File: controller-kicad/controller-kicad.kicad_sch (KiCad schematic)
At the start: 97 parts

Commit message: Finishing up ECU schematic
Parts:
- removed C? (x3): 10nF, symbol Device:C_Small
- removed R?: 10K, symbol Device:R_Small
- removed U?: PC817, Package_DIP:DIP-4_W7.62mm, symbol Isolator:PC817
- removed U?: MCP1416, Package_TO_SOT_SMD:SOT-23-5, symbol Driver_FET:MCP1416
- added C1, C2: 27pF, symbol Device:C_Small
- added C24, C26, C28, C36, C38: 10nF, symbol Device:C_Small
- added C31, C32, C33, C34: 10pF DNP, symbol Device:C_Small
- added C35: 22nF, symbol Device:C_Small
- added C37: 100nF, symbol Device:C_Small
- added FB1, FB2: FerriteBead_Small, symbol Device:FerriteBead_Small
- added J1: RJ45_Amphenol_RJMG1BD3B8K1ANR, Connector_RJ:RJ45_Amphenol_RJMG1BD3B8K1ANR, symbol Connector:RJ45_Amphenol_RJMG1BD3B8K1ANR
- added J11: Conn_01x02_Female, symbol Connector:Conn_01x02_Female
- added R22: 1.5K, symbol Device:R_Small
- added R24: 750, symbol Device:R_Small
- added R32: 1K, symbol Device:R_Small
- added R33: 1M, symbol Device:R_Small
- added R34: 350, symbol Device:R_Small
- added U11: TL431DBZ, Package_TO_SOT_SMD:SOT-23, symbol Reference_Voltage:TL431DBZ
- added U12: AD8495, Package_SO:MSOP-8_3x3mm_P0.65mm, symbol Sensor_Temperature:AD8495
- added U13: TLP250, Package_DIP:DIP-8_W7.62mm, symbol Driver_FET:TLP250
- added Y1: 25 MHz, symbol Device:Crystal
- gave numbers to parts that had none: 91
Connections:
- net +3.3V: now also C24.1, C26.1, C28.1, C35.2, FB2.2, J1.R4 (TCT), J1.R5 (RCT), R24.2, R32.2, U12.7 (+Vs); no longer C42.1, U15.2 (VO)
- net +5V: now also FB1.2; no longer C41.1, U14.2 (VO)
- net ADC3_IN7: now also U12.5 (SENSE), U12.6
- net ADC3_IN8: now also R22.1, R24.1
- net ETH_LED1: now also J1.L4 (LEDG_A)
- net ETH_LED2: now also J1.L1 (LEDY_A)
- net GND: now also C1.1, C2.1, C24.2, C26.2, C28.2, C31.2, C32.2, C33.2, C34.2, C35.1, C36.1, C38.2, J1.L2 (LEDY_K), J1.L3 (LEDG_K), R22.2, R33.2, U11.3 (A), U12.3 (-Vs), U13.3 (C)
- net SPARK: now also U13.6 (VO)
- net SPARK_CTRL: now also R34.1
- net SPARK_GND: now also U13.5 (VEE)
- net SPARK_VCC: now also U13.8 (VCC)
- net Vdrive: now also J4.2 (Pin_2), J5.2 (Pin_2)
- net at R23.2, U6.20 (TXN): now also C31.1, J1.R2 (TD-)
- net at R25.2, U6.21 (TXP): now also C32.1, J1.R1 (TD+)
- net at R28.2, U6.22 (RXN): now also C33.1, J1.R6 (RD-)
- net at R31.2, U6.23 (RXP): now also C34.1, J1.R3 (RD+)
- net at U1.23 (PH0): now also C1.2, Y1.2
- net at U1.24 (PH1): now also C2.2, Y1.1
- new net: R32.1, U11.1 (K), U11.2 (REF), U12.2 (REF)
- new net: C42.1, FB2.1, U15.2 (VO)
- new net: C41.1, FB1.1, U14.2 (VO)
- new net: R34.2, U13.2 (A)
- new net Earth: J1.13 (SHIELD), J1.R8 (GND)
- new net TS1+: C36.2, C37.1, J11.1 (Pin_1), U12.8 (+IN)
- new net TS1-: C37.2, C38.1, J11.2 (Pin_2), R33.1, U12.1 (-IN)
- no-connect marks 0 -> 91
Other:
- moved on the sheet: C18, C20, C21, C22, C39, C40, C41, C42, D1, D2, D3, D4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

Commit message: Started routing PCB
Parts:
- removed C13, C15: 2.2uF, symbol Device:C_Small
- removed FB2: FerriteBead_Small, symbol Device:FerriteBead_Small
- added C1, C4: 2.2uF, Capacitor_SMD:C_0603_1608Metric_Pad1.08x0.95mm_HandSolder, symbol Device:C_Small
- added J12: Conn_01x01, Connector_PinHeader_2.54mm:PinHeader_1x01_P2.54mm_Vertical, symbol Connector_Generic:Conn_01x01
- added R16: 10K, Resistor_SMD:R_0603_1608Metric_Pad0.98x0.95mm_HandSolder, symbol Device:R_Small
- C10: renamed from C8; footprint (none) -> Capacitor_SMD:C_0603_1608Metric_Pad1.08x0.95mm_HandSolder
- C11: renamed from C9; footprint (none) -> Capacitor_SMD:C_0603_1608Metric_Pad1.08x0.95mm_HandSolder
- C12: renamed from C10; footprint (none) -> Capacitor_SMD:C_0603_1608Metric_Pad1.08x0.95mm_HandSolder
- C13: renamed from C11; footprint (none) -> Capacitor_SMD:C_0603_1608Metric_Pad1.08x0.95mm_HandSolder
- C14: renamed from C12; footprint (none) -> Capacitor_SMD:C_0603_1608Metric_Pad1.08x0.95mm_HandSolder
- C15: renamed from C14; footprint (none) -> Capacitor_SMD:C_0603_1608Metric_Pad1.08x0.95mm_HandSolder
- C16, C17, C18, C19, C20, C21, C22, C23, C24, C25, C26, C27, C28, C29, C30, C31, C32, C33, C34, C35, C36, C37, C38, C39, C40, C41, C42, FB1: footprint (none) -> Capacitor_SMD:C_0603_1608Metric_Pad1.08x0.95mm_HandSolder
- C2: renamed from C1; footprint (none) -> Capacitor_SMD:C_0603_1608Metric_Pad1.08x0.95mm_HandSolder
- C3: renamed from C2; footprint (none) -> Capacitor_SMD:C_0603_1608Metric_Pad1.08x0.95mm_HandSolder
- C5: renamed from C3; footprint (none) -> Capacitor_SMD:C_0603_1608Metric_Pad1.08x0.95mm_HandSolder
- C6: renamed from C4; footprint (none) -> Capacitor_SMD:C_0603_1608Metric_Pad1.08x0.95mm_HandSolder
- C7: renamed from C5; footprint (none) -> Capacitor_SMD:C_0603_1608Metric_Pad1.08x0.95mm_HandSolder
- C8: renamed from C6; footprint (none) -> Capacitor_SMD:C_0603_1608Metric_Pad1.08x0.95mm_HandSolder
- C9: renamed from C7; footprint (none) -> Capacitor_SMD:C_0603_1608Metric_Pad1.08x0.95mm_HandSolder
- D1, D2, D5, D6: footprint (none) -> Diode_SMD:D_SMA_Handsoldering
- D3, D4, D7, D8: footprint (none) -> Diode_SMD:D_SMA-SMB_Universal_Handsoldering
- J10, J6, J7, J8, J9: footprint (none) -> Connector_JST:JST_PH_B3B-PH-K_1x03_P2.00mm_Vertical
- J11, J2, J3, J4, J5: footprint (none) -> Connector_JST:JST_PH_B2B-PH-K_1x02_P2.00mm_Vertical
- J13: renamed from J12; footprint (none) -> Connector_JST:JST_VH_B3P-VH-B_1x03_P3.96mm_Vertical
- J14: renamed from J13; footprint (none) -> Connector_JST:JST_PH_B5B-PH-K_1x05_P2.00mm_Vertical
- R1, R10, R14, R15, R2, R3, R4, R5, R8, R9: footprint (none) -> Resistor_SMD:R_0603_1608Metric_Pad0.98x0.95mm_HandSolder
- R11, R12, R13: value 10 -> 33; footprint (none) -> Resistor_SMD:R_0603_1608Metric_Pad0.98x0.95mm_HandSolder
- R17: renamed from R16; footprint (none) -> Resistor_SMD:R_0603_1608Metric_Pad0.98x0.95mm_HandSolder
- R18: renamed from R17; footprint (none) -> Resistor_SMD:R_0603_1608Metric_Pad0.98x0.95mm_HandSolder
- R19: renamed from R18; footprint (none) -> Resistor_SMD:R_0603_1608Metric_Pad0.98x0.95mm_HandSolder
- R20: renamed from R19; footprint (none) -> Resistor_SMD:R_0603_1608Metric_Pad0.98x0.95mm_HandSolder
- R21: renamed from R20; footprint (none) -> Resistor_SMD:R_0603_1608Metric_Pad0.98x0.95mm_HandSolder
- R22: renamed from R21; footprint (none) -> Resistor_SMD:R_0603_1608Metric_Pad0.98x0.95mm_HandSolder
- R23: renamed from R22; footprint (none) -> Resistor_SMD:R_0603_1608Metric_Pad0.98x0.95mm_HandSolder
- R24: renamed from R23; footprint (none) -> Resistor_SMD:R_0603_1608Metric_Pad0.98x0.95mm_HandSolder
- R25: renamed from R24; footprint (none) -> Resistor_SMD:R_0603_1608Metric_Pad0.98x0.95mm_HandSolder
- R26: renamed from R25; footprint (none) -> Resistor_SMD:R_0603_1608Metric_Pad0.98x0.95mm_HandSolder
- R27: renamed from R26; footprint (none) -> Resistor_SMD:R_0603_1608Metric_Pad0.98x0.95mm_HandSolder
- R28: renamed from R27; footprint (none) -> Resistor_SMD:R_0603_1608Metric_Pad0.98x0.95mm_HandSolder
- R29: renamed from R28; footprint (none) -> Resistor_SMD:R_0603_1608Metric_Pad0.98x0.95mm_HandSolder
- R30: renamed from R29; footprint (none) -> Resistor_SMD:R_0603_1608Metric_Pad0.98x0.95mm_HandSolder
- R31: renamed from R30; footprint (none) -> Resistor_SMD:R_0603_1608Metric_Pad0.98x0.95mm_HandSolder
- R32: renamed from R31; footprint (none) -> Resistor_SMD:R_0603_1608Metric_Pad0.98x0.95mm_HandSolder
- R33: renamed from R32; footprint (none) -> Resistor_SMD:R_0603_1608Metric_Pad0.98x0.95mm_HandSolder
- R34: renamed from R33; footprint (none) -> Resistor_SMD:R_0603_1608Metric_Pad0.98x0.95mm_HandSolder
- R35: renamed from R34; footprint (none) -> Resistor_SMD:R_0603_1608Metric_Pad0.98x0.95mm_HandSolder
- R6, R7: value 100 -> 150; footprint (none) -> Resistor_SMD:R_0603_1608Metric_Pad0.98x0.95mm_HandSolder
- U10, U4, U5, U9: footprint (none) -> Package_TO_SOT_SMD:TO-252-3_TabPin2
- U6: footprint (none) -> Package_DFN_QFN:VQFN-24-1EP_4x4mm_P0.5mm_EP2.45x2.45mm
- Y1, Y2: footprint (none) -> Crystal:Crystal_SMD_HC49-SD_HandSoldering
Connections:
- net +12V: now also FB1.1; no longer J13.2 (Pin_2)
- net +3.3V: now also C42.1, U15.2 (VO), R16.2
- net +5V: now also C41.1, U14.2 (VO); no longer FB1.2
- net Earth: now also J12.1 (Pin_1)
- net GND: now also C1.1, C4.1
- net RST: no longer U6.15 (~{RST})
- net VCAP_1: no longer names the net of U1.71 (VCAP_1)
- net VCAP_1: now also C4.2
- net VCAP_2: no longer names the net of U1.106 (VCAP_2)
- net VCAP_2: now also C1.2
- new net: FB1.2, J13.2 (Pin_2)
- new net: R16.1, U6.15 (~{RST})
- no-connect marks 91 -> 92

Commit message: More progress on routing
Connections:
- net ETH_RXD0: now also R12.2; no longer R12.1, R4.1
- net ETH_RXD1: no longer R3.1
- net at U6.8 (RXD0): now also R12.1, R4.1; no longer R12.2
- net at R11.2, U6.7 (RXD1): now also R3.1
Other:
- moved on the sheet: C18, C22, R3, R4

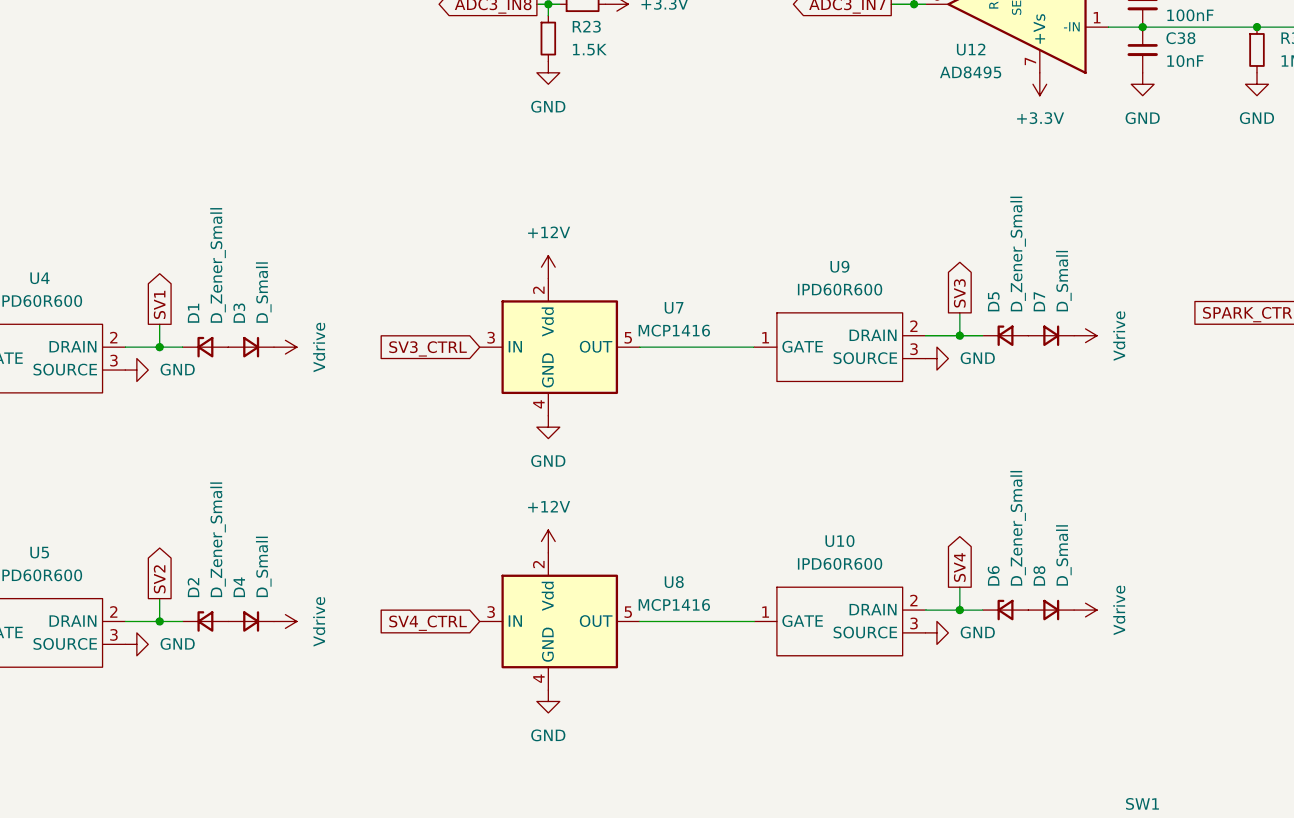
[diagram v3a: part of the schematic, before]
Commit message: Got all components onto PCB
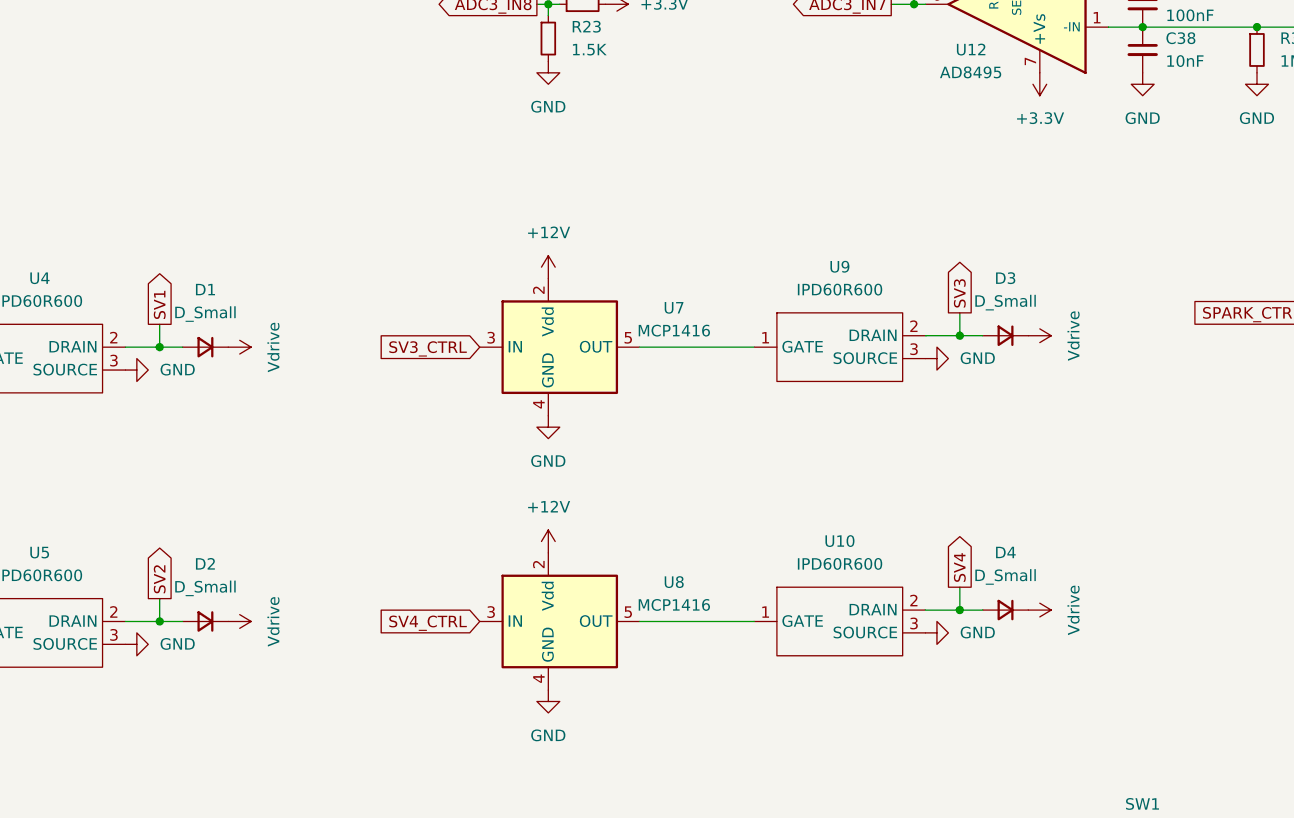
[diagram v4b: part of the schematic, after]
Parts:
- removed D1, D2, D5, D6: D_Zener_Small, Diode_SMD:D_SMA_Handsoldering, symbol Device:D_Zener_Small
- J10, J6, J7, J8, J9: footprint Connector_JST:JST_PH_B3B-PH-K_1x03_P2.00mm_Vertical -> Connector_JST:JST_PH_S3B-PH-SM4-TB_1x03-1MP_P2.00mm_Horizontal
- J11, J2, J3, J4, J5: footprint Connector_JST:JST_PH_B2B-PH-K_1x02_P2.00mm_Vertical -> Connector_JST:JST_PH_S2B-PH-SM4-TB_1x02-1MP_P2.00mm_Horizontal
- renumbered D3 to D1, D4 to D2, D7 to D3, D8 to D4
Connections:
- net SV1: now also D1.2 (A)
- net SV2: now also D2.2 (A)
- net SV3: now also D3.2 (A)
- net SV4: now also D4.2 (A)
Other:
- moved on the sheet: D1, D2, D3, D4

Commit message: Routing mostly finished
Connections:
- net SPARK: now also J6.2 (Pin_2); no longer J6.3 (Pin_3)
- net SPARK_GND: now also J6.3 (Pin_3); no longer J6.2 (Pin_2)
- net TX+: now reaches C32.1, J1.R1 (TD+), R26.2, U6.21 (TXP)
- net TX-: now reaches C31.1, J1.R2 (TD-), R24.2, U6.20 (TXN)
- net RX+: now reaches C34.1, J1.R3 (RD+), R32.2, U6.23 (RXP)
- net RX-: now reaches C33.1, J1.R6 (RD-), R29.2, U6.22 (RXN)
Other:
- moved on the sheet: C31, C32, C33, C34

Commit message: Added reset button to PCB
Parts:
- SW1: footprint (none) -> Button_Switch_SMD:SW_SPST_PTS810
- U10, U4, U5, U9: footprint Package_TO_SOT_SMD:TO-252-3_TabPin2 -> custom_footprints:TO-252-3_TabPin2-HandSolder
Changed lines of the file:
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@@
     (property "Reference" "U4" (id 0) (at 183.515 165.1 0))
     (property "Value" "IPD60R600" (id 1) (at 183.515 167.64 0))
-    (property "Footprint" "Package_TO_SOT_SMD:TO-252-3_TabPin2" (id 2) (at 182.88 173.99 0)
+    (property "Footprint" "custom_footprints:TO-252-3_TabPin2-HandSolder" (id 2) (at 182.88 173.99 0)
       (effects (font (size 1.27 1.27)) hide)
     )
@@
     (property "Reference" "SW1" (id 0) (at 306.07 223.52 0))
     (property "Value" "SW_RST" (id 1) (at 306.07 226.06 0))
-    (property "Footprint" "" (id 2) (at 306.07 229.87 0)
+    (property "Footprint" "Button_Switch_SMD:SW_SPST_PTS810" (id 2) (at 306.07 229.87 0)
       (effects (font (size 1.27 1.27)) hide)
     )
@@
     (property "Reference" "U10" (id 0) (at 272.415 194.31 0))
     (property "Value" "IPD60R600" (id 1) (at 272.415 196.85 0))
-    (property "Footprint" "Package_TO_SOT_SMD:TO-252-3_TabPin2" (id 2) (at 271.78 203.2 0)
+    (property "Footprint" "custom_footprints:TO-252-3_TabPin2-HandSolder" (id 2) (at 271.78 203.2 0)
       (effects (font (size 1.27 1.27)) hide)
     )
@@
     (property "Reference" "U5" (id 0) (at 183.515 195.58 0))
     (property "Value" "IPD60R600" (id 1) (at 183.515 198.12 0))
-    (property "Footprint" "Package_TO_SOT_SMD:TO-252-3_TabPin2" (id 2) (at 182.88 204.47 0)
+    (property "Footprint" "custom_footprints:TO-252-3_TabPin2-HandSolder" (id 2) (at 182.88 204.47 0)
       (effects (font (size 1.27 1.27)) hide)
     )
@@
     (property "Reference" "U9" (id 0) (at 272.415 163.83 0))
     (property "Value" "IPD60R600" (id 1) (at 272.415 166.37 0))
-    (property "Footprint" "Package_TO_SOT_SMD:TO-252-3_TabPin2" (id 2) (at 271.78 172.72 0)
+    (property "Footprint" "custom_footprints:TO-252-3_TabPin2-HandSolder" (id 2) (at 271.78 172.72 0)
       (effects (font (size 1.27 1.27)) hide)
     )
@@
     )
     (path "/8ffcde6d-fd07-4359-9d96-9271c4d5b26a"
-      (reference "SW1") (unit 1) (value "SW_RST") (footprint "")
+      (reference "SW1") (unit 1) (value "SW_RST") (footprint "Button_Switch_SMD:SW_SPST_PTS810")
     )
     (path "/d083db5d-69ed-42a1-933b-c404b23d2906"
@@
     )
     (path "/747a404d-9901-435d-ad56-606c72d7d017"
-      (reference "U4") (unit 1) (value "IPD60R600") (footprint "Package_TO_SOT_SMD:TO-252-3_TabPin2")
+      (reference "U4") (unit 1) (value "IPD60R600") (footprint "custom_footprints:TO-252-3_TabPin2-HandSolder")
     )
     (path "/9b30c0cf-e39f-4685-835b-2f74ae6bee9c"
-      (reference "U5") (unit 1) (value "IPD60R600") (footprint "Package_TO_SOT_SMD:TO-252-3_TabPin2")
+      (reference "U5") (unit 1) (value "IPD60R600") (footprint "custom_footprints:TO-252-3_TabPin2-HandSolder")
     )
     (path "/536095e5-415f-4d02-8525-1cde9017551b"
@@
     )
     (path "/ddc3771c-ab50-44d4-a609-5481aceed088"
-      (reference "U9") (unit 1) (value "IPD60R600") (footprint "Package_TO_SOT_SMD:TO-252-3_TabPin2")
+      (reference "U9") (unit 1) (value "IPD60R600") (footprint "custom_footprints:TO-252-3_TabPin2-HandSolder")
     )
     (path "/995fe23b-aa10-45ad-9960-db202a942cfd"
-      (reference "U10") (unit 1) (value "IPD60R600") (footprint "Package_TO_SOT_SMD:TO-252-3_TabPin2")
+      (reference "U10") (unit 1) (value "IPD60R600") (footprint "custom_footprints:TO-252-3_TabPin2-HandSolder")
     )
     (path "/236d2f26-c372-429c-954f-5d54e6855352"

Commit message: Hopefully finished board
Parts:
- added D5: LED_Small, LED_SMD:LED_0603_1608Metric_Pad1.05x0.95mm_HandSolder, symbol Device:LED_Small
- added J15: Conn_01x03_Female, Connector_JST:JST_PH_S3B-PH-SM4-TB_1x03-1MP_P2.00mm_Horizontal, symbol Connector:Conn_01x03_Female
- added R36: 220, Resistor_SMD:R_0603_1608Metric_Pad0.98x0.95mm_HandSolder, symbol Device:R_Small
- C2, C3: value 27pF -> 23pF
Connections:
- net +3.3V: no longer R25.2
- net +5V: now also J15.1 (Pin_1)
- net GND: now also J15.3 (Pin_3), R36.2
- net at U1.4 (PE5): now also D5.2 (A)
- new net: D5.1 (K), R36.1
- new net PS5: J15.2 (Pin_2), R25.2
- no-connect marks 92 -> 91
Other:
- moved on the sheet: J11, J12, R23, R25, R35, SW1, U13
